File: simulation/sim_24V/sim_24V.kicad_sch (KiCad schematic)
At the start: 20 parts, among them Q1 2N7000

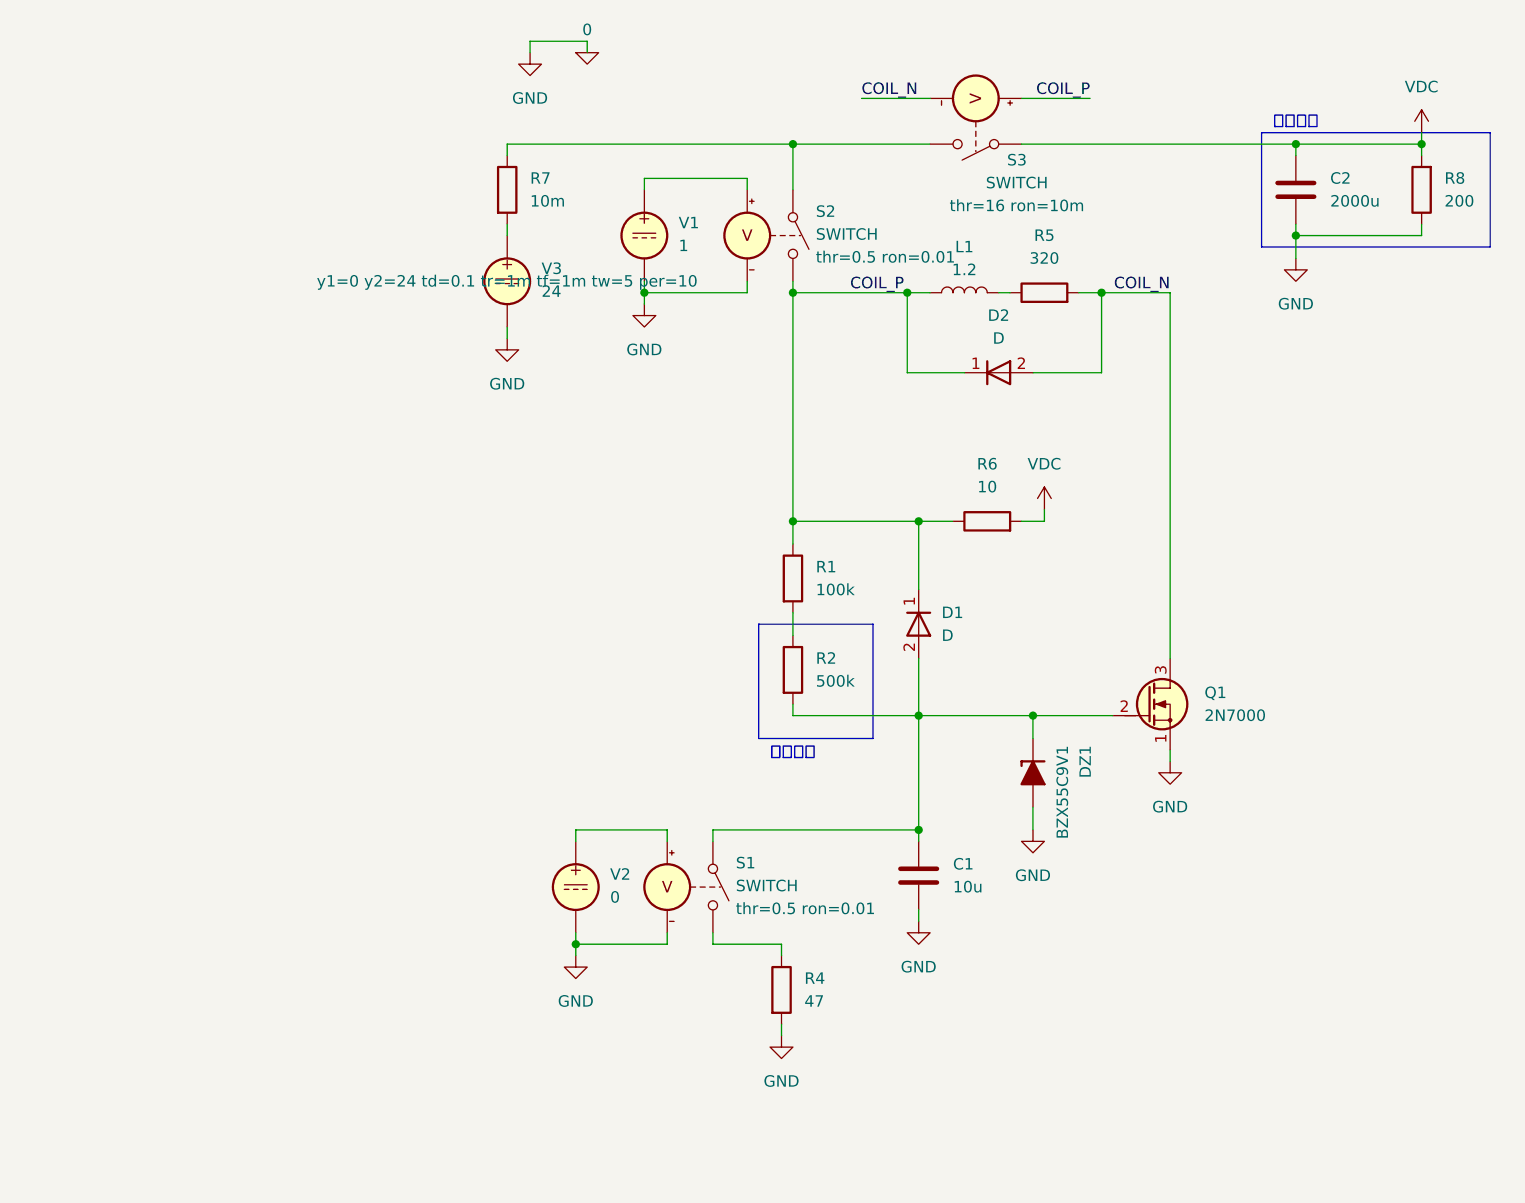
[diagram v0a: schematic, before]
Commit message: 24V基板　スロースタート回路のシミュレーションに正帰還回路を追加 これにより，ゲート電圧が急激に上がるようになり，リレーの発振やMOSFETの発熱を抑えることができるはず．
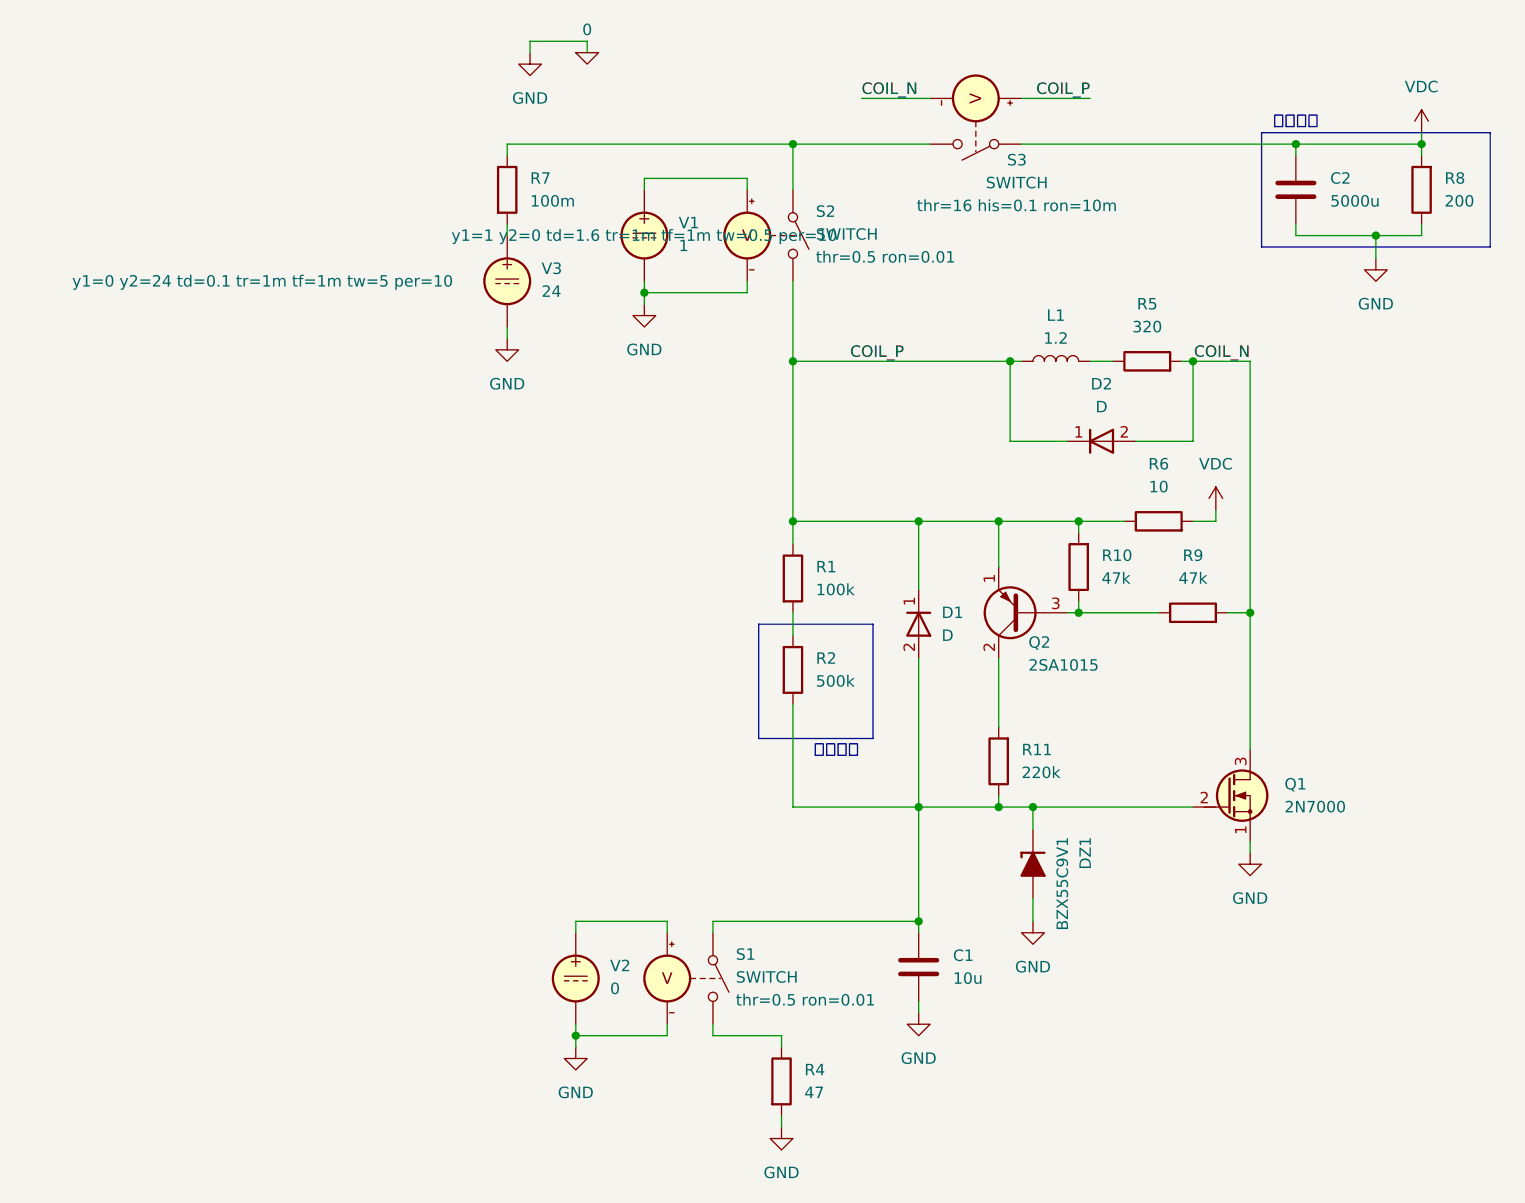
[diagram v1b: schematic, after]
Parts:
- added Q2: 2SA1015, Package_TO_SOT_THT:TO-92_Inline, symbol Transistor_BJT:2SA1015
- added R10, R9: 47k, symbol Device:R
- added R11: 220k, symbol Device:R
- C2: value 2000u -> 5000u
- R7: value 10m -> 100m
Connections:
- net COIL_N: now also R9.2
- net COIL_P: now also Q2.1 (E), R10.2
- net at C1.1, D1.2 (A), DZ1.1 (K)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: now also R11.1
- new net: Q2.3 (B), R10.1, R9.1
- new net: Q2.2 (C), R11.2
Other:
- moved on the sheet: C1, D2, DZ1, L1, Q1, R4, R5, R6, S1, V2

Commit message: 24V基板　スロースタートのシミュにフェイルセーフ機構を追加 非常停止スイッチを想定したS1とS2がどちらも切断された場合，リレーが切れず非常停止が発生しない不具合があった
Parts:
- added D3: D, symbol Simulation_SPICE:D
- added R3: 100k, symbol Device:R
- R2: value 500k -> 300k
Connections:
- net 0: now also R3.2
- net COIL_P: now also D3.2 (A); no longer R6.1
- net at C1.1, D1.2 (A), DZ1.1 (K)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: now also R3.1
- new net: D3.1 (K), R6.1
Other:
- moved on the sheet: Q1, R6

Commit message: 24V基板　シミュレーションの回路を実際の回路に適応した．また，放電抵抗を取り外した． スロースタート用コンデンサの常時放電抵抗があることにより，可変抵抗の抵抗値を上げた際にスロースタートが解除されないことが分かった．放電用ダイオードもあるため，放電抵抗は消した．
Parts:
- removed R3: 100k, symbol Device:R
- R2: value 300k -> 1000k
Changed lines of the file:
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@@
-	)
-	(junction
-		(at 91.44 109.22)
-		(diameter 0)
-		(color 0 0 0 0)
 	)
 	(junction
@@
 	(wire
 		(pts
-			(xy 91.44 119.38) (xy 91.44 121.92)
-		)
-		(stroke
-			(width 0)
-			(type default)
-		)
-	)
-	(wire
-		(pts
 			(xy 123.19 44.45) (xy 123.19 45.72)
 		)
@@
 	(wire
 		(pts
-			(xy 91.44 109.22) (xy 114.3 109.22)
-		)
-		(stroke
-			(width 0)
-			(type default)
-		)
-	)
-	(wire
-		(pts
 			(xy 67.31 92.71) (xy 67.31 109.22)
 		)
@@
 	(wire
 		(pts
-			(xy 80.01 109.22) (xy 91.44 109.22)
+			(xy 80.01 109.22) (xy 114.3 109.22)
 		)
 		(stroke
@@
 		(pts
 			(xy 118.11 45.72) (xy 109.22 45.72)
-		)
-		(stroke
-			(width 0)
-			(type default)
-		)
-	)
-	(wire
-		(pts
-			(xy 91.44 109.22) (xy 91.44 111.76)
 		)
 		(stroke
@@
 			)
 			(justify left bottom)
-		)
-	)
-	(symbol
-		(lib_id "power:GND")
-		(at 91.44 121.92 0)
-		(unit 1)
-		(body_style 1)
-		(exclude_from_sim no)
-		(in_bom yes)
-		(on_board yes)
-		(in_pos_files yes)
-		(dnp no)
-		(fields_autoplaced yes)
-		(property "Reference" "#PWR010"
-			(at 91.44 128.27 0)
-			(hide yes)
-			(show_name no)
-			(do_not_autoplace no)
-			(effects
-				(font
-					(size 1.27 1.27)
-				)
-			)
-		)
-		(property "Value" "GND"
-			(at 91.44 127 0)
-			(show_name no)
-			(do_not_autoplace no)
-			(effects
-				(font
-					(size 1.27 1.27)
-				)
-			)
-		)
-		(property "Footprint" ""
-			(at 91.44 121.92 0)
-			(hide yes)
-			(show_name no)
-			(do_not_autoplace no)
-			(effects
-				(font
-					(size 1.27 1.27)
-				)
-			)
-		)
-		(property "Datasheet" ""
-			(at 91.44 121.92 0)
-			(hide yes)
-			(show_name no)
-			(do_not_autoplace no)
-			(effects
-				(font
-					(size 1.27 1.27)
-				)
-			)
-		)
-		(property "Description" "Power symbol creates a global label with name \"GND\" , ground"
-			(at 91.44 121.92 0)
-			(hide yes)
-			(show_name no)
-			(do_not_autoplace no)
-			(effects
-				(font
-					(size 1.27 1.27)
-				)
-			)
-		)
-		(pin "1"
-		)
-		(instances
-			(project "sim_24V"
-				(path "/346af76c-4be7-4209-82c4-0da454b641fa"
-					(reference "#PWR010")
-					(unit 1)
-				)
-			)
 		)
 	)
@@
 			)
 		)
-		(property "Value" "300k"
+		(property "Value" "1000k"
 			(at 55.88 95.2499 0)
 			(show_name no)
@@
 	)
 	(symbol
-		(lib_id "Device:R")
-		(at 91.44 115.57 0)
-		(unit 1)
-		(body_style 1)
-		(exclude_from_sim no)
-		(in_bom yes)
-		(on_board yes)
-		(in_pos_files yes)
-		(dnp no)
-		(fields_autoplaced yes)
-		(property "Reference" "R3"
-			(at 93.98 114.2999 0)
-			(show_name no)
-			(do_not_autoplace no)
-			(effects
-				(font
-					(size 1.27 1.27)
-				)
-				(justify left)
-			)
-		)
-		(property "Value" "100k"
-			(at 93.98 116.8399 0)
-			(show_name no)
-			(do_not_autoplace no)
-			(effects
-				(font
-					(size 1.27 1.27)
-				)
-				(justify left)
-			)
-		)
-		(property "Footprint" ""
-			(at 89.662 115.57 90)
-			(hide yes)
-			(show_name no)
-			(do_not_autoplace no)
-			(effects
-				(font
-					(size 1.27 1.27)
-				)
-			)
-		)
-		(property "Datasheet" ""
-			(at 91.44 115.57 0)
-			(hide yes)
-			(show_name no)
-			(do_not_autoplace no)
-			(effects
-				(font
-					(size 1.27 1.27)
-				)
-			)
-		)
-		(property "Description" "Resistor"
-			(at 91.44 115.57 0)
-			(hide yes)
-			(show_name no)
-			(do_not_autoplace no)
-			(effects
-				(font
-					(size 1.27 1.27)
-				)
-			)
-		)
-		(pin "2"
-		)
-		(pin "1"
-		)
-		(instances
-			(project "sim_24V"
-				(path "/346af76c-4be7-4209-82c4-0da454b641fa"
-					(reference "R3")
-					(unit 1)
-				)
-			)
-		)
-	)
-	(symbol
 		(lib_id "Simulation_SPICE:D")
 		(at 87.63 68.58 0)
@@
 			)
 		)
-		(property "Sim.Params" "y1=0 y2=0 td=1.6 tr=1m tf=1m tw=5 per=10"
+		(property "Sim.Params" "y1=0 y2=0 td=3.2 tr=1m tf=1m tw=5 per=10"
 			(at 29.21 128.27 0)
 			(hide yes)
